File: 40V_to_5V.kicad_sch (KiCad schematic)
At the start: 6 parts, among them U601 XL1509-5.0

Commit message: WIP
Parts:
- C122: JLCPCB Part # C125977 -> C116211; Partnumber UWT1H221MNL1GS -> UCD1H221MNL1GS
- C122: value 180u 35V -> 220uF 10V; footprint Capacitor_SMD:CP_Elec_10x12.6 -> Capacitor_Tantalum_SMD:CP_EIA-7343-31_Kemet-D; JLCPCB Part # C488000 -> C2690543; Manufacturer Nichicon -> CEC(Shenzhen Zhenhua XinYun Elec); Partnumber PCV1V181MCL2GS -> PXTD010M227E040STU
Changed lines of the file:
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@@
   )
   (label "VOUT" (at 113.665 49.53 0) (fields_autoplaced)
-    (effects (font (size 1.27 1.27)) (justify left bottom))
+    (effects (font (size 1 1)) (justify left bottom))
   )
   (hierarchical_label "GND" (shape bidirectional) (at 123.19 59.69 270) (fields_autoplaced)
@@
     (in_bom yes) (on_board yes) (dnp no) (fields_autoplaced)
     (property "Reference" "D8" (at 125.095 53.086 90)
-      (effects (font (size 1.27 1.27)) (justify left))
+      (effects (font (size 1 1)) (justify left))
     )
     (property "Value" "SS34" (at 125.095 55.626 90)
-      (effects (font (size 1.27 1.27)) (justify left))
+      (effects (font (size 1 1)) (justify left))
     )
     (property "Footprint" "Diode_SMD:D_SMA" (at 123.19 54.61 90)
@@
       (project "stm32f4_uno"
         (path "/e63e39d7-6ac0-4ffd-8aa3-1841a4541b55/c71f752d-6d24-44fb-bd6d-69f95efd2cf1"
-          (reference "D601") (unit 1)
+          (reference "D501") (unit 1)
         )
       )
@@
     (in_bom yes) (on_board yes) (dnp no) (fields_autoplaced)
     (property "Reference" "L602" (at 135.255 44.45 90)
-      (effects (font (size 1.27 1.27)))
+      (effects (font (size 1 1)))
     )
     (property "Value" "68uH 3A" (at 135.255 46.99 90)
-      (effects (font (size 1.27 1.27)))
+      (effects (font (size 1 1)))
     )
     (property "Footprint" "Inductor_SMD:L_Chilisin_BMRG00101030" (at 135.255 49.53 0)
@@
       (project "stm32f4_uno"
         (path "/e63e39d7-6ac0-4ffd-8aa3-1841a4541b55/c71f752d-6d24-44fb-bd6d-69f95efd2cf1"
-          (reference "L601") (unit 1)
+          (reference "L501") (unit 1)
         )
       )
@@
     (in_bom yes) (on_board yes) (dnp no) (fields_autoplaced)
     (property "Reference" "U601" (at 103.505 42.545 0)
-      (effects (font (size 1.27 1.27)))
+      (effects (font (size 1 1)))
     )
     (property "Value" "XL1509-5.0" (at 103.505 45.085 0)
-      (effects (font (size 1.27 1.27)))
+      (effects (font (size 1 1)))
     )
     (property "Footprint" "Package_SO:SOIC-8_3.9x4.9mm_P1.27mm" (at 103.505 43.688 0)
@@
       (project "stm32f4_uno"
         (path "/e63e39d7-6ac0-4ffd-8aa3-1841a4541b55/c71f752d-6d24-44fb-bd6d-69f95efd2cf1"
-          (reference "U602") (unit 1)
+          (reference "U501") (unit 1)
         )
       )
@@
       (project "stm32f4_uno"
         (path "/e63e39d7-6ac0-4ffd-8aa3-1841a4541b55/c71f752d-6d24-44fb-bd6d-69f95efd2cf1"
-          (reference "C604") (unit 1)
+          (reference "C501") (unit 1)
         )
       )
@@
   (symbol (lib_id "Device:C_Polarized_Small") (at 61.595 53.975 0) (unit 1)
     (in_bom yes) (on_board yes) (dnp no)
-    (property "Reference" "C122" (at 67.31 52.07 0)
-      (effects (font (size 1.27 1.27)) (justify right))
-    )
-    (property "Value" "220u 50V" (at 71.755 56.515 0)
-      (effects (font (size 1.27 1.27)) (justify right))
+    (property "Reference" "C122" (at 62.23 52.07 0)
+      (effects (font (size 1 1)) (justify left))
+    )
+    (property "Value" "220u 50V" (at 62.23 55.88 0)
+      (effects (font (size 1 1)) (justify left))
     )
     (property "Footprint" "Capacitor_SMD:CP_Elec_10x10" (at 61.595 53.975 0)
@@
       (effects (font (size 1.27 1.27)) hide)
     )
-    (property "Description" "220uF 50V 220mA@120Hz ±20% SMD,D10xL10mm  Aluminum Electrolytic Capacitors - SMD ROHS" (at 61.595 53.975 0)
+    (property "Description" "220uF 50V 350mA@120Hz ±20% SMD,D10xL10mm  Aluminum Electrolytic Capacitors - SMD ROHS" (at 61.595 53.975 0)
       (effects (font (size 1.27 1.27)) hide)
     )
@@
       (effects (font (size 1.27 1.27)) hide)
     )
-    (property "Partnumber" "UWT1H221MNL1GS" (at 61.595 53.975 0)
-      (effects (font (size 1.27 1.27)) hide)
-    )
-    (property "JLCPCB Part #" "C125977" (at 61.595 53.975 0)
+    (property "Partnumber" "UCD1H221MNL1GS" (at 61.595 53.975 0)
+      (effects (font (size 1.27 1.27)) hide)
+    )
+    (property "JLCPCB Part #" "C116211" (at 61.595 53.975 0)
       (effects (font (size 1.27 1.27)) hide)
     )
@@
       (project "stm32f4_uno"
         (path "/e63e39d7-6ac0-4ffd-8aa3-1841a4541b55/c71f752d-6d24-44fb-bd6d-69f95efd2cf1"
-          (reference "C603") (unit 1)
+          (reference "C502") (unit 1)
         )
       )
@@
   (symbol (lib_id "Device:C_Polarized_Small") (at 151.765 54.61 0) (unit 1)
     (in_bom yes) (on_board yes) (dnp no)
-    (property "Reference" "C122" (at 157.48 52.705 0)
-      (effects (font (size 1.27 1.27)) (justify right))
-    )
-    (property "Value" "180u 35V" (at 161.925 57.15 0)
-      (effects (font (size 1.27 1.27)) (justify right))
-    )
-    (property "Footprint" "Capacitor_SMD:CP_Elec_10x12.6" (at 151.765 54.61 0)
-      (effects (font (size 1.27 1.27)) hide)
-    )
-    (property "Datasheet" "https://datasheet.lcsc.com/lcsc/2002251108_Nichicon-PCV1V181MCL2GS_C488000.pdf" (at 151.765 54.61 0)
-      (effects (font (size 1.27 1.27)) hide)
-    )
-    (property "Description" "180uF 35V 4.1A@100kHz 22mΩ@100kHz ±20% SMD,D10xL12.7mm  Aluminum Electrolytic Capacitors - SMD ROHS" (at 151.765 54.61 0)
-      (effects (font (size 1.27 1.27)) hide)
-    )
-    (property "Manufacturer" "Nichicon" (at 151.765 54.61 0)
-      (effects (font (size 1.27 1.27)) hide)
-    )
-    (property "Partnumber" "PCV1V181MCL2GS" (at 151.765 54.61 0)
-      (effects (font (size 1.27 1.27)) hide)
-    )
-    (property "JLCPCB Part #" "C488000" (at 151.765 54.61 0)
+    (property "Reference" "C122" (at 152.4 52.705 0)
+      (effects (font (size 1 1)) (justify left))
+    )
+    (property "Value" "220uF 10V" (at 152.4 56.515 0)
+      (effects (font (size 1 1)) (justify left))
+    )
+    (property "Footprint" "Capacitor_Tantalum_SMD:CP_EIA-7343-31_Kemet-D" (at 151.765 54.61 0)
+      (effects (font (size 1.27 1.27)) hide)
+    )
+    (property "Datasheet" "https://datasheet.lcsc.com/lcsc/2102221641_CEC-Shenzhen-Zhenhua-XinYun-Elec-PXTD010M227E040STU_C2690543.pdf" (at 151.765 54.61 0)
+      (effects (font (size 1.27 1.27)) hide)
+    )
+    (property "Description" "220uF 10V ±20% CASE-D-7343 Tantalum Capacitors ROHS" (at 151.765 54.61 0)
+      (effects (font (size 1.27 1.27)) hide)
+    )
+    (property "Manufacturer" "CEC(Shenzhen Zhenhua XinYun Elec)" (at 151.765 54.61 0)
+      (effects (font (size 1.27 1.27)) hide)
+    )
+    (property "Partnumber" "PXTD010M227E040STU" (at 151.765 54.61 0)
+      (effects (font (size 1.27 1.27)) hide)
+    )
+    (property "JLCPCB Part #" "C2690543" (at 151.765 54.61 0)
       (effects (font (size 1.27 1.27)) hide)
     )
@@
       (project "stm32f4_uno"
         (path "/e63e39d7-6ac0-4ffd-8aa3-1841a4541b55/c71f752d-6d24-44fb-bd6d-69f95efd2cf1"
-          (reference "C605") (unit 1)
-        )
-      )
+          (reference "C503") (unit 1)
+        )
+      )

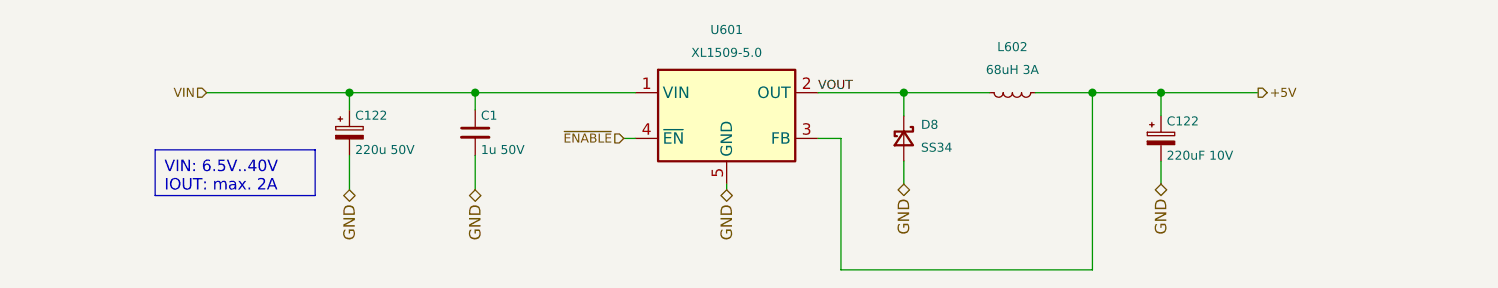
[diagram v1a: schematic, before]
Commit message: Replaced 5V LDO for a 40V->5V buck converter
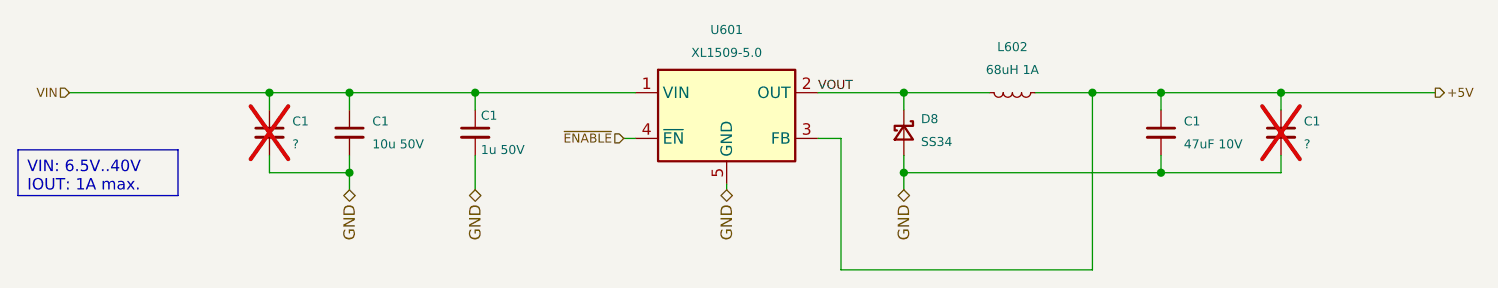
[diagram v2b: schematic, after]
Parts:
- removed C122: 220u 50V, Capacitor_SMD:CP_Elec_10x10, symbol Device:C_Polarized_Small
- removed C122: 220uF 10V, Capacitor_Tantalum_SMD:CP_EIA-7343-31_Kemet-D, symbol Device:C_Polarized_Small
- added C1 (x2): ?, Capacitor_THT:CP_Radial_D6.3mm_P2.50mm, symbol Device:C_Small
- added C1: 47uF 10V, Capacitor_SMD:C_1206_3216Metric, symbol Device:C_Small
- added C1: 10u 50V, Capacitor_SMD:C_1206_3216Metric, symbol Device:C_Small
- L602: value 68uH 3A -> 68uH 1A; footprint Inductor_SMD:L_Chilisin_BMRG00101030 -> Inductor_SMD:L_Sunlord_SWPA6045S; JLCPCB Part # C497902 -> C142105; Manufacturer YJYCOIN -> Chilisin Elec; Partnumber YSPI1050-680M -> LVS606045-680M-AU
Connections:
- net +5V: now also C1.1, C1.1
- net GND: now also C1.2, C1.2, C1.2, C1.2
- net VIN: now also C1.1, C1.1
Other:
- moved on the sheet: D8

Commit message: #2 Add silkscreen texts
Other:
- company: (none) -> easy-smart solution GmbH
- title: (none) -> STM32F4 Uno
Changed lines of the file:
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@@
 (kicad_sch (version 20230121) (generator eeschema)
   (paper "A4")
+  (title_block
+    (title "STM32F4 Uno")
+    (date "2023-10-02")
+    (rev "1.0.x-dev")
+    (company "easy-smart solution GmbH")
+  )
   (junction (at 144.145 49.53) (diameter 0) (color 0 0 0 0)
   )
